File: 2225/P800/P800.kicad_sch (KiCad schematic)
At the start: 0 parts

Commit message: Created initial P800 schematic
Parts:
- added C802: 0.01u, symbol Device:C
- added C803, C804, C809: 470u, symbol Device:C_Polarized_US
- added C805: 100u, symbol Device:C_Polarized_US
- added C806: 0.047u, symbol Device:C
- added C807: 0.04u, symbol Device:C
- added C808: 3.3u, symbol Device:C_Polarized_US
- added D801, D802, D803, D804: 1N4002, Diode_THT:D_DO-41_SOD81_P10.16mm_Horizontal, symbol Diode:1N4002
- added F801: Fuse, symbol Device:Fuse
- added H805: TIP41C, Package_TO_SOT_THT:TO-220-3_Vertical, symbol Transistor_BJT:TIP41C
- added H806: 2N3055, Package_TO_SOT_THT:TO-3, symbol Transistor_BJT:2N3055
- added H807: 1N53xxB, Diode_THT:D_DO-201_P15.24mm_Horizontal, symbol Diode:1N53xxB
- added R801: 22, symbol Device:R_US
- added R803, R804: 1.5k, symbol Device:R_US
- added R805: 330, symbol Device:R_US
- added R806: 36k, symbol Device:R_US
- added R807: 27k, symbol Device:R_US
- added R808: R_Potentiometer_US, symbol Device:R_Potentiometer_US
- added V1: VSOURCE, symbol pspice:VSOURCE
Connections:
- new net: C805.1, R803.1, R804.2
- new net: C804.1, H805.2 (C), R801.2, R803.2
- new net: R806.1, R808.3
- new net: C808.1, H805.3 (E), R805.2, R806.2
- new net: C808.2, H806.1 (B), R808.2
- new net: C807.1, C809.1, H806.2 (E), H807.1 (K), R805.1
- new net: C806.1, H805.1 (B), H806.3 (C), R804.1
- new net: C803.1, D803.1 (K), D804.1 (K), R801.1
- new net: C802.1, D801.1 (K), D803.2 (A), F801.2
- new net: R807.2, R808.1
- new net: F801.1, V1.1 (E1)
- new net: C802.2, D802.1 (K), D804.2 (A), V1.2 (E2)
- new net GND: C803.2, C804.2, C805.2, C806.2, C807.2, C809.2, D801.2 (A), D802.2 (A), H807.2 (A), R807.1

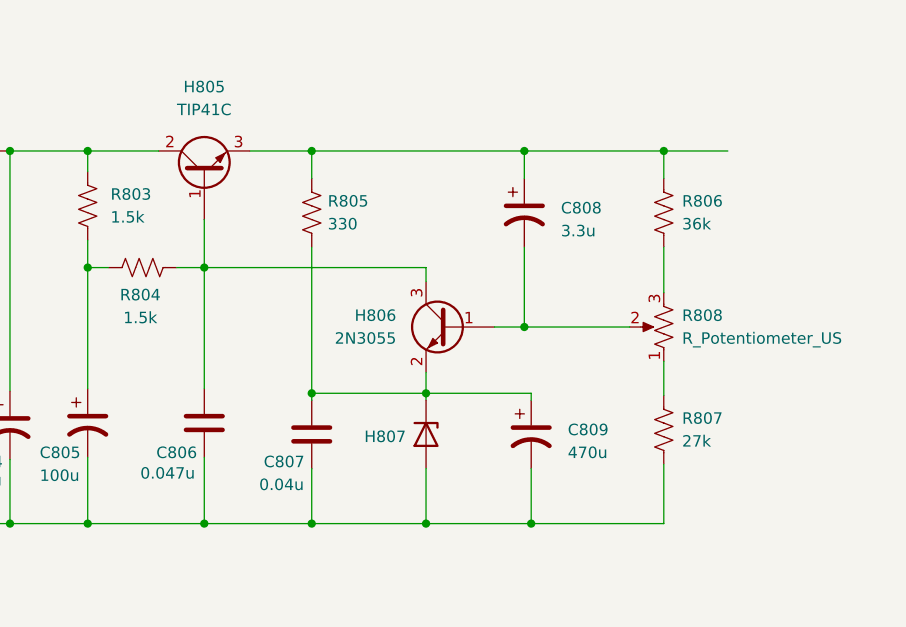
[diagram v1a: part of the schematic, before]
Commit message: Added model files for Zener diode, transistors, and trim pot
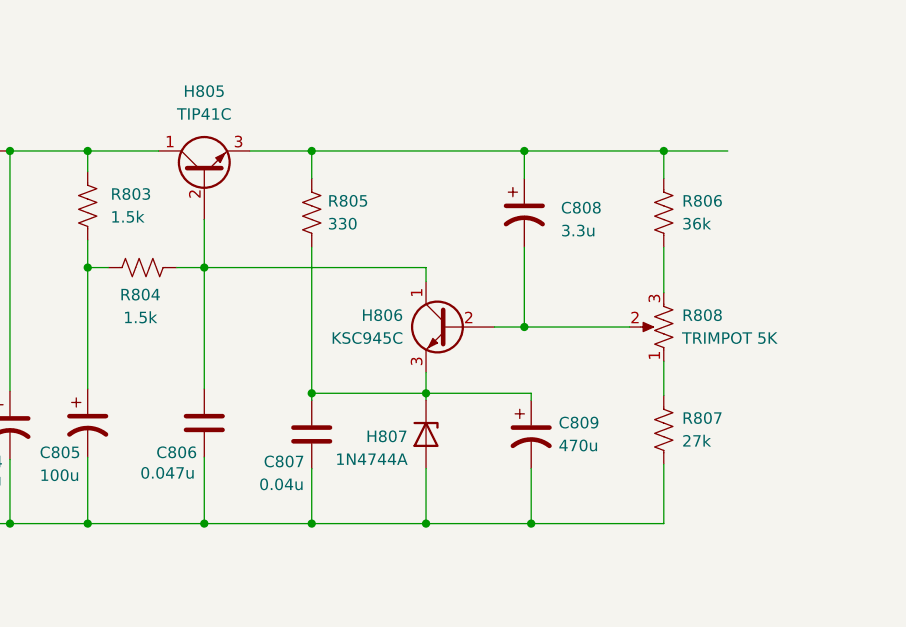
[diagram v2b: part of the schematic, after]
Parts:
- removed H805: TIP41C, Package_TO_SOT_THT:TO-220-3_Vertical, symbol Transistor_BJT:TIP41C
- removed H806: 2N3055, Package_TO_SOT_THT:TO-3, symbol Transistor_BJT:2N3055
- removed H807: 1N53xxB, Diode_THT:D_DO-201_P15.24mm_Horizontal, symbol Diode:1N53xxB
- added H805: TIP41C, symbol Device:Q_NPN_CBE
- added H806: KSC945C, symbol Device:Q_NPN_CBE
- added H807: 1N4744A, Diode_THT:D_DO-41_SOD81_P10.16mm_Horizontal, symbol Diode:1N47xxA
- F801: Spice_Netlist_Enabled (none) -> N; Spice_Primitive (none) -> R
- R808: value R_Potentiometer_US -> TRIMPOT 5K; Spice_Lib_File (none) -> models/spice/linear_potentiometer.lib; Spice_Model (none) -> POT_LINEAR; Spice_Netlist_Enabled (none) -> Y; Spice_Primitive (none) -> X
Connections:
- net GND: now also H807.2 (A)
- net at C804.1, R801.2, R803.2: now also H805.1 (C)
- net at C808.1, R805.2, R806.2: now also H805.3 (E)
- net at C808.2, R808.2: now also H806.2 (B)
- net at C807.1, C809.1, R805.1: now also H806.3 (E), H807.1 (K)
- net at C806.1, R804.1: now also H805.2 (B), H806.1 (C)
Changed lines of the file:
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@@
     (stroke (width 0) (type default) (color 0 0 0 0))
   )
+  (symbol (lib_id "Device:Q_NPN_CBE") (at 174.752 92.71 0) (mirror y) (unit 1)
+    (in_bom yes) (on_board yes) (fields_autoplaced)
+    (property "Reference" "H806" (id 0) (at 169.672 91.4399 0)
+      (effects (font (size 1.27 1.27)) (justify left))
+    )
+    (property "Value" "KSC945C" (id 1) (at 169.672 93.9799 0)
+      (effects (font (size 1.27 1.27)) (justify left))
+    )
+    (property "Footprint" "" (id 2) (at 169.672 90.17 0)
+      (effects (font (size 1.27 1.27)) hide)
+    )
+    (property "Datasheet" "~" (id 3) (at 174.752 92.71 0)
+      (effects (font (size 1.27 1.27)) hide)
+    )
+    (property "Spice_Primitive" "Q" (id 4) (at 174.752 92.71 0)
+      (effects (font (size 1.27 1.27)) hide)
+    )
+    (property "Spice_Model" "KSC945" (id 5) (at 174.752 92.71 0)
+      (effects (font (size 1.27 1.27)) hide)
+    )
+    (property "Spice_Netlist_Enabled" "Y" (id 6) (at 174.752 92.71 0)
+      (effects (font (size 1.27 1.27)) hide)
+    )
+    (property "Spice_Lib_File" "models/spice/QKSC945.lib" (id 7) (at 174.752 92.71 0)
+      (effects (font (size 1.27 1.27)) hide)
+    )
+    (pin "1")
+    (pin "2")
+    (pin "3")
+  )
   (symbol (lib_id "Device:C_Polarized_US") (at 134.62 103.378 0) (unit 1)
     (in_bom yes) (on_board yes)
@@
   (symbol (lib_id "Device:C_Polarized_US") (at 183.896 104.648 0) (unit 1)
     (in_bom yes) (on_board yes)
-    (property "Reference" "C809" (id 0) (at 187.96 104.14 0)
-      (effects (font (size 1.27 1.27)) (justify left))
-    )
-    (property "Value" "470u" (id 1) (at 187.96 106.68 0)
+    (property "Reference" "C809" (id 0) (at 186.944 103.378 0)
+      (effects (font (size 1.27 1.27)) (justify left))
+    )
+    (property "Value" "470u" (id 1) (at 186.944 105.918 0)
       (effects (font (size 1.27 1.27)) (justify left))
     )
@@
     (pin "2")
   )
-  (symbol (lib_id "Transistor_BJT:2N3055") (at 174.752 92.71 0) (mirror y) (unit 1)
-    (in_bom yes) (on_board yes) (fields_autoplaced)
-    (property "Reference" "H806" (id 0) (at 168.91 91.4399 0)
-      (effects (font (size 1.27 1.27)) (justify left))
-    )
-    (property "Value" "2N3055" (id 1) (at 168.91 93.9799 0)
-      (effects (font (size 1.27 1.27)) (justify left))
-    )
-    (property "Footprint" "Package_TO_SOT_THT:TO-3" (id 2) (at 169.672 94.615 0)
-      (effects (font (size 1.27 1.27) italic) (justify left) hide)
-    )
-    (property "Datasheet" "http://www.onsemi.com/pub_link/Collateral/2N3055-D.PDF" (id 3) (at 174.752 92.71 0)
-      (effects (font (size 1.27 1.27)) (justify left) hide)
-    )
-    (property "Spice_Primitive" "Q" (id 4) (at 174.752 92.71 0)
-      (effects (font (size 1.27 1.27)) hide)
-    )
-    (property "Spice_Model" "2N3055" (id 5) (at 174.752 92.71 0)
-      (effects (font (size 1.27 1.27)) hide)
-    )
-    (property "Spice_Netlist_Enabled" "Y" (id 6) (at 174.752 92.71 0)
-      (effects (font (size 1.27 1.27)) hide)
-    )
-    (property "Spice_Node_Sequence" "3 1 2" (id 7) (at 174.752 92.71 0)
+  (symbol (lib_id "Device:Q_NPN_CBE") (at 147.574 75.692 90) (unit 1)
+    (in_bom yes) (on_board yes) (fields_autoplaced)
+    (property "Reference" "H805" (id 0) (at 147.574 66.548 90))
+    (property "Value" "TIP41C" (id 1) (at 147.574 69.088 90))
+    (property "Footprint" "" (id 2) (at 145.034 70.612 0)
+      (effects (font (size 1.27 1.27)) hide)
+    )
+    (property "Datasheet" "~" (id 3) (at 147.574 75.692 0)
+      (effects (font (size 1.27 1.27)) hide)
+    )
+    (property "Spice_Primitive" "Q" (id 4) (at 147.574 75.692 0)
+      (effects (font (size 1.27 1.27)) hide)
+    )
+    (property "Spice_Model" "TIP41C" (id 5) (at 147.574 75.692 0)
+      (effects (font (size 1.27 1.27)) hide)
+    )
+    (property "Spice_Netlist_Enabled" "Y" (id 6) (at 147.574 75.692 0)
+      (effects (font (size 1.27 1.27)) hide)
+    )
+    (property "Spice_Lib_File" "models/spice/QTIP41C.lib" (id 7) (at 147.574 75.692 0)
       (effects (font (size 1.27 1.27)) hide)
     )
@@
       (effects (font (size 1.27 1.27)) (justify right))
     )
-    (property "Value" "R_Potentiometer_US" (id 1) (at 200.66 93.9799 0)
+    (property "Value" "TRIMPOT 5K" (id 1) (at 200.66 93.9799 0)
       (effects (font (size 1.27 1.27)) (justify right))
     )
@@
     )
     (property "Datasheet" "~" (id 3) (at 198.628 92.71 0)
+      (effects (font (size 1.27 1.27)) hide)
+    )
+    (property "Spice_Primitive" "X" (id 4) (at 198.628 92.71 0)
+      (effects (font (size 1.27 1.27)) hide)
+    )
+    (property "Spice_Model" "POT_LINEAR" (id 5) (at 198.628 92.71 0)
+      (effects (font (size 1.27 1.27)) hide)
+    )
+    (property "Spice_Netlist_Enabled" "Y" (id 6) (at 198.628 92.71 0)
+      (effects (font (size 1.27 1.27)) hide)
+    )
+    (property "Spice_Lib_File" "models/spice/linear_potentiometer.lib" (id 7) (at 198.628 92.71 0)
       (effects (font (size 1.27 1.27)) hide)
     )
@@
       (effects (font (size 1.27 1.27)) hide)
     )
+    (property "Spice_Primitive" "R" (id 4) (at 80.772 65.278 0)
+      (effects (font (size 1.27 1.27)) hide)
+    )
+    (property "Spice_Netlist_Enabled" "N" (id 5) (at 80.772 65.278 0)
+      (effects (font (size 1.27 1.27)) hide)
+    )
     (pin "1")
     (pin "2")
@@
     (pin "2")
   )
-  (symbol (lib_id "Transistor_BJT:TIP41C") (at 147.574 75.692 90) (unit 1)
-    (in_bom yes) (on_board yes) (fields_autoplaced)
-    (property "Reference" "H805" (id 0) (at 147.574 66.04 90))
-    (property "Value" "TIP41C" (id 1) (at 147.574 68.58 90))
-    (property "Footprint" "Package_TO_SOT_THT:TO-220-3_Vertical" (id 2) (at 149.479 69.342 0)
-      (effects (font (size 1.27 1.27) italic) (justify left) hide)
-    )
-    (property "Datasheet" "https://www.centralsemi.com/get_document.php?cmp=1&mergetype=pd&mergepath=pd&pdf_id=tip41.PDF" (id 3) (at 147.574 75.692 0)
-      (effects (font (size 1.27 1.27)) (justify left) hide)
-    )
-    (property "Spice_Primitive" "Q" (id 4) (at 147.574 75.692 0)
-      (effects (font (size 1.27 1.27)) hide)
-    )
-    (property "Spice_Model" "TIP41C" (id 5) (at 147.574 75.692 0)
-      (effects (font (size 1.27 1.27)) hide)
-    )
-    (property "Spice_Netlist_Enabled" "Y" (id 6) (at 147.574 75.692 0)
-      (effects (font (size 1.27 1.27)) hide)
-    )
-    (property "Spice_Node_Sequence" "2 1 3" (id 7) (at 147.574 75.692 0)
-      (effects (font (size 1.27 1.27)) hide)
-    )
-    (pin "1")
-    (pin "2")
-    (pin "3")
-  )
-  (symbol (lib_id "Diode:1N53xxB") (at 172.212 104.648 270) (unit 1)
-    (in_bom yes) (on_board yes)
-    (property "Reference" "H807" (id 0) (at 165.354 104.902 90)
-      (effects (font (size 1.27 1.27)) (justify left))
-    )
-    (property "Value" "1N53xxB" (id 1) (at 166.37 107.696 90)
-      (effects (font (size 1.27 1.27)) (justify left) hide)
-    )
-    (property "Footprint" "Diode_THT:D_DO-201_P15.24mm_Horizontal" (id 2) (at 167.767 104.648 0)
-      (effects (font (size 1.27 1.27)) hide)
-    )
-    (property "Datasheet" "https://diotec.com/tl_files/diotec/files/pdf/datasheets/1n5345b.pdf" (id 3) (at 172.212 104.648 0)
+  (symbol (lib_id "Diode:1N47xxA") (at 172.212 104.648 270) (unit 1)
+    (in_bom yes) (on_board yes)
+    (property "Reference" "H807" (id 0) (at 170.18 104.902 90)
+      (effects (font (size 1.27 1.27)) (justify right))
+    )
+    (property "Value" "1N4744A" (id 1) (at 170.18 107.442 90)
+      (effects (font (size 1.27 1.27)) (justify right))
+    )
+    (property "Footprint" "Diode_THT:D_DO-41_SOD81_P10.16mm_Horizontal" (id 2) (at 167.767 104.648 0)
+      (effects (font (size 1.27 1.27)) hide)
+    )
+    (property "Datasheet" "https://www.vishay.com/docs/85816/1n4728a.pdf" (id 3) (at 172.212 104.648 0)
+      (effects (font (size 1.27 1.27)) hide)
+    )
+    (property "Spice_Primitive" "D" (id 4) (at 172.212 104.648 0)
+      (effects (font (size 1.27 1.27)) hide)
+    )
+    (property "Spice_Model" "1N4744A" (id 5) (at 172.212 104.648 0)
+      (effects (font (size 1.27 1.27)) hide)
+    )
+    (property "Spice_Netlist_Enabled" "Y" (id 6) (at 172.212 104.648 0)
+      (effects (font (size 1.27 1.27)) hide)
+    )
+    (property "Spice_Node_Sequence" "2 1" (id 7) (at 172.212 104.648 0)
+      (effects (font (size 1.27 1.27)) hide)
+    )
+    (property "Spice_Lib_File" "models/spice/D1N4744A.lib" (id 8) (at 172.212 104.648 0)
       (effects (font (size 1.27 1.27)) hide)
     )
@@
       (reference "F801") (unit 1) (value "Fuse") (footprint "")
     )
-    (path "/bfa9d2d8-0bc7-47d7-851a-e5608c5a4e60"
-      (reference "H805") (unit 1) (value "TIP41C") (footprint "Package_TO_SOT_THT:TO-220-3_Vertical")
-    )
-    (path "/2da7c607-0fa6-41c0-9534-456c3922d751"
-      (reference "H806") (unit 1) (value "2N3055") (footprint "Package_TO_SOT_THT:TO-3")
-    )
-    (path "/d716e336-c1ba-49ac-88d6-94f070c4be86"
-      (reference "H807") (unit 1) (value "1N53xxB") (footprint "Diode_THT:D_DO-201_P15.24mm_Horizontal")
+    (path "/2cd51694-aca3-43a0-b01b-16ebb3d155fd"
+      (reference "H805") (unit 1) (value "TIP41C") (footprint "")
+    )
+    (path "/0472fef0-a765-4685-87a8-c1fb4ec1b984"
+      (reference "H806") (unit 1) (value "KSC945C") (footprint "")
+    )
+    (path "/c1f0f6e8-70a3-4d8f-8aba-0998b5419a68"
+      (reference "H807") (unit 1) (value "1N4744A") (footprint "Diode_THT:D_DO-41_SOD81_P10.16mm_Horizontal")
     )
     (path "/df5cd730-38c8-4566-bd22-84849e955ad4"
@@
     )
     (path "/8cebcc18-95de-4f41-97fa-568ed920743e"
-      (reference "R808") (unit 1) (value "R_Potentiometer_US") (footprint "")
+      (reference "R808") (unit 1) (value "TRIMPOT 5K") (footprint "")
     )
     (path "/d914d498-1494-40e2-935b-79bbf7d638c5"

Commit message: Created diode bridge components (P800 H801:H804) in project-specific symbol library; updated schematic to include H803 & H804
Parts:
- removed D801, D802, D803, D804: 1N4002, Diode_THT:D_DO-41_SOD81_P10.16mm_Horizontal, symbol Diode:1N4002
- added H803: MBRF10150CTR, Package_TO_SOT_THT:TO-220-3_Vertical, symbol P800:MBRF10150CTR
- added H804: MBRF10150CT, Package_TO_SOT_THT:TO-220-3_Vertical, symbol P800:MBRF10150CT
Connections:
- net GND: now also H803.2
- net at C803.1, R801.1: now also H804.2
- net at C802.1, F801.2: now also H803.3, H804.3
- net at C802.2, V1.2 (E2): now also H803.1, H804.1
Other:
- moved on the sheet: C802, F801, V1

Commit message: Added model file (subckt) for diode bridges P800 H803 & H804
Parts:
- F801: Spice_Model (none) -> Fuse
- H803: Spice_Lib_File (none) -> models/spice/DMBRF10150CT.lib; Spice_Model (none) -> DIODE_PAIR_CA; Spice_Netlist_Enabled (none) -> Y; Spice_Primitive (none) -> X
- H804: Spice_Lib_File (none) -> models/spice/DMBRF10150CT.lib; Spice_Model (none) -> DIODE_PAIR_CC; Spice_Netlist_Enabled (none) -> Y; Spice_Primitive (none) -> X
- R808: Spice_Model POT_LINEAR -> LINEAR_POTENTIOMETER POT_VAL=5k SET=0.5
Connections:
- net P800_OUT_35VDC: now reaches C808.1, H805.3 (E), R805.2, R806.2
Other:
- note added: ".model 1N4744A D"
- note added: ".tran 0.1m 60m 0"
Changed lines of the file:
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@@
     (stroke (width 0) (type default) (color 0 0 0 0))
+  )
+  (text ".model 1N4744A D" (at 167.386 117.602 0)
+    (effects (font (size 1.27 1.27)) (justify left bottom))
+  )
+  (text ".tran 0.1m 60m 0" (at 62.992 96.52 0)
+    (effects (font (size 1.27 1.27)) (justify left bottom))
+  )
+  (global_label "P800_OUT_35VDC" (shape output) (at 205.74 73.152 0) (fields_autoplaced)
+    (effects (font (size 1.27 1.27)) (justify left))
+    (property "Intersheet References" "${INTERSHEET_REFS}" (id 0) (at 224.6631 73.0726 0)
+      (effects (font (size 1.27 1.27)) (justify left) hide)
+    )
   )
   (symbol (lib_id "Device:Q_NPN_CBE") (at 174.752 92.71 0) (mirror y) (unit 1)
@@
       (effects (font (size 1.27 1.27)) hide)
     )
+    (property "Spice_Primitive" "X" (id 4) (at 95.25 73.152 0)
+      (effects (font (size 1.27 1.27)) hide)
+    )
+    (property "Spice_Model" "DIODE_PAIR_CA" (id 5) (at 95.25 73.152 0)
+      (effects (font (size 1.27 1.27)) hide)
+    )
+    (property "Spice_Netlist_Enabled" "Y" (id 6) (at 95.25 73.152 0)
+      (effects (font (size 1.27 1.27)) hide)
+    )
+    (property "Spice_Lib_File" "models/spice/DMBRF10150CT.lib" (id 7) (at 95.25 73.152 0)
+      (effects (font (size 1.27 1.27)) hide)
+    )
     (pin "1")
     (pin "2")
@@
       (effects (font (size 1.27 1.27)) hide)
     )
+    (property "Spice_Primitive" "X" (id 4) (at 105.664 73.152 0)
+      (effects (font (size 1.27 1.27)) hide)
+    )
+    (property "Spice_Model" "DIODE_PAIR_CC" (id 5) (at 105.664 73.152 0)
+      (effects (font (size 1.27 1.27)) hide)
+    )
+    (property "Spice_Netlist_Enabled" "Y" (id 6) (at 105.664 73.152 0)
+      (effects (font (size 1.27 1.27)) hide)
+    )
+    (property "Spice_Lib_File" "models/spice/DMBRF10150CT.lib" (id 7) (at 105.664 73.152 0)
+      (effects (font (size 1.27 1.27)) hide)
+    )
     (pin "1")
     (pin "2")
@@
       (effects (font (size 1.27 1.27)) hide)
     )
-    (property "Spice_Model" "POT_LINEAR" (id 5) (at 198.628 92.71 0)
+    (property "Spice_Model" "LINEAR_POTENTIOMETER POT_VAL=5k SET=0.5" (id 5) (at 198.628 92.71 0)
       (effects (font (size 1.27 1.27)) hide)
     )
@@
       (effects (font (size 1.27 1.27)) hide)
     )
+    (property "Spice_Model" "Fuse" (id 6) (at 79.248 64.516 0)
+      (effects (font (size 1.27 1.27)) hide)
+    )
